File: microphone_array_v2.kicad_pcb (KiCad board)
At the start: 4 copper layers, 120 x 120 mm, 134 parts, among them J1 RPi_P1_26, J2 Tang_Nano_9K, J3 Tang_Nano_9K, U1 LP5907MFX-3.3, U2 SN74LVC244A, U3 USBLC6-4SC6, U4 USBLC6-4SC6, X1 24.576MHz

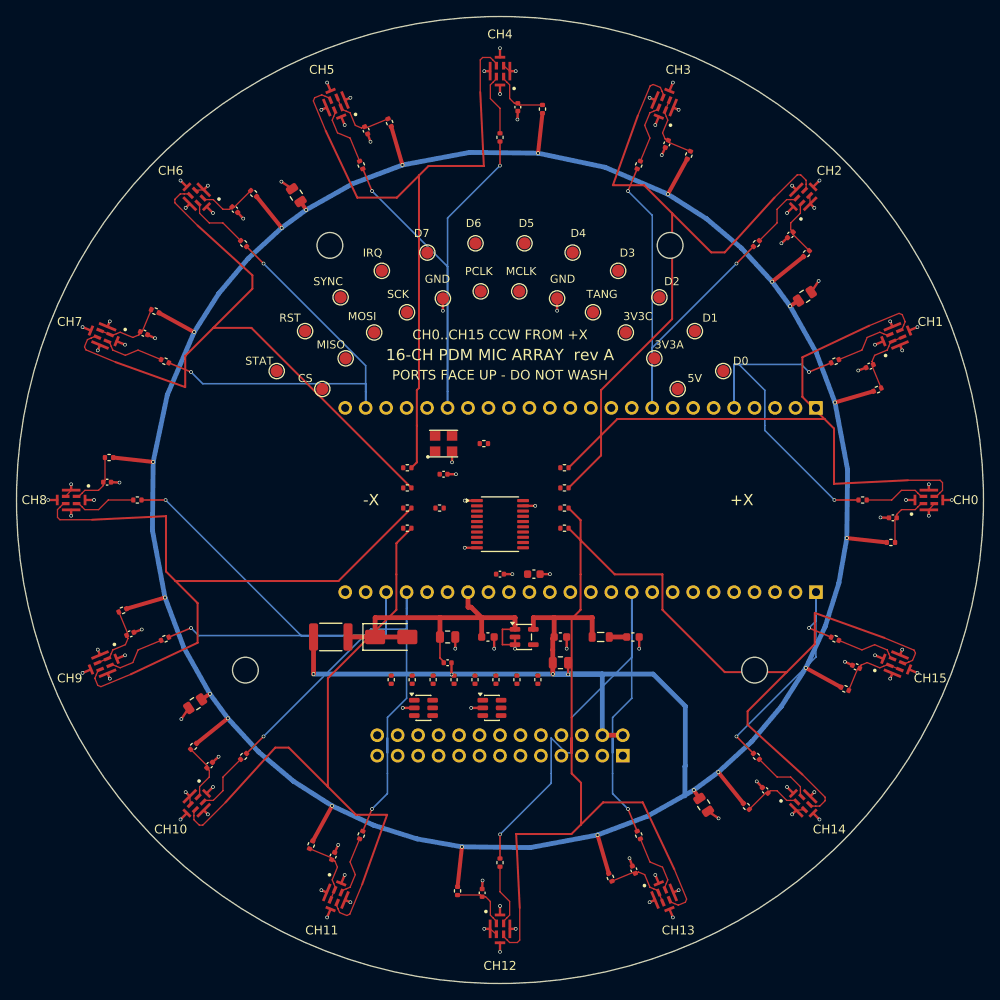
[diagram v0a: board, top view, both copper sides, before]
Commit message: Asked Claude to remove routes that hit each other, then it ran out of tokens
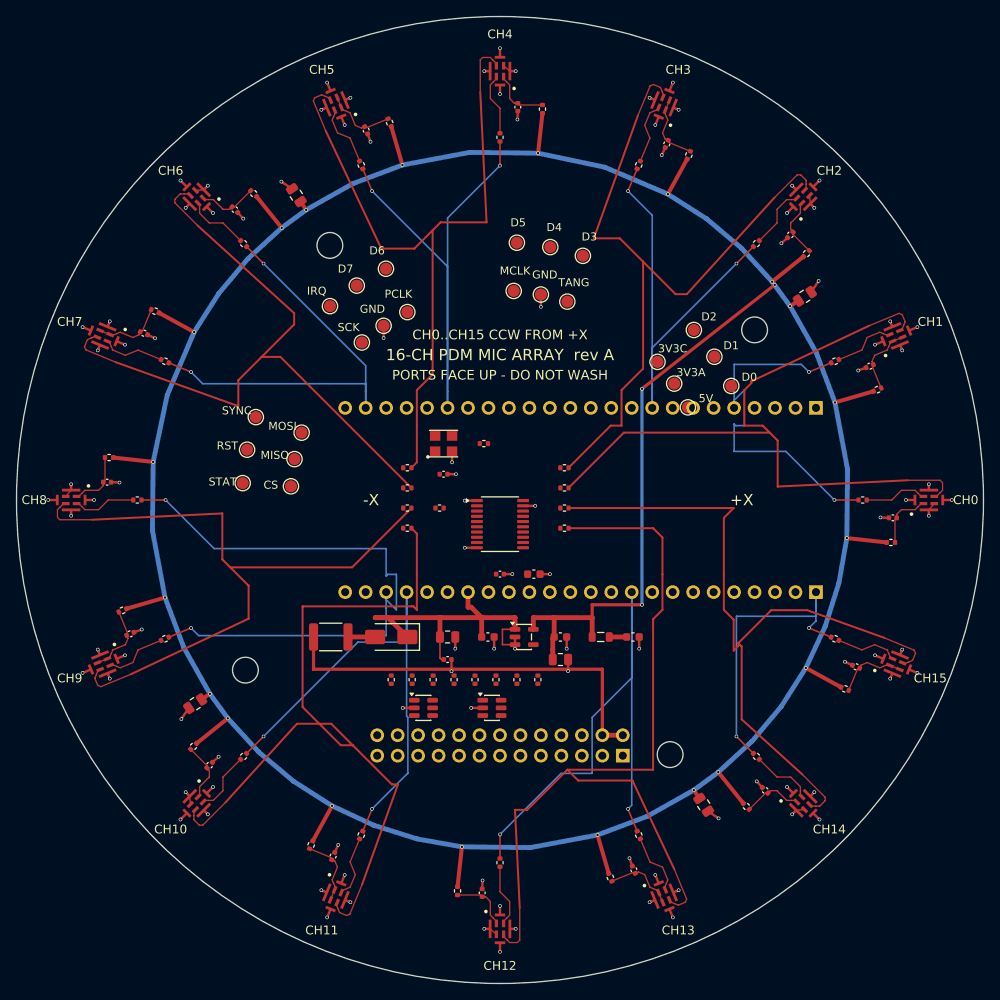
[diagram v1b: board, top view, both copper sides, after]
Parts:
- moved TP22 18.2 mm to (119.7, 139.7)
- moved TP23 16.4 mm to (118.6, 143.8)
- moved TP10 15.4 mm to (125.4, 141.6)
- moved H1 14.8 mm to (181.6, 128.9)
- moved H4 14.8 mm to (171.1, 181.6)
- moved TP24 14.5 mm to (118.1, 147.9)
- moved TP11 14.0 mm to (124.5, 144.9)
- moved TP12 12.7 mm to (124.1, 148.3)
- moved TP19 11.6 mm to (135.8, 121.3)
- moved TP20 9.67 mm to (132.2, 123.4)
- moved TP7 9.47 mm to (138.5, 126.7)
- moved TP8 8.10 mm to (135.6, 128.4)
- moved TP21 7.79 mm to (128.9, 125.9)
- moved TP9 6.74 mm to (132.9, 130.5)
- moved TP15 5.89 mm to (174.1, 128.9)
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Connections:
- U2 pad 12: PDM_CLK_Y7 -> PDM_CLK_Y6
- U2 pad 14: PDM_CLK_Y6 -> PDM_CLK_Y7
- U2 pad 16: PDM_CLK_Y1 -> PDM_CLK_Y0
- U2 pad 18: PDM_CLK_Y0 -> PDM_CLK_Y1
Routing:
- net +3V3A: track 404.1 -> 431.0 mm, vias 21 -> 23
- net PDM_CLK_B5: track 85.5 -> 100.9 mm
- net PDM_CLK_B6: track 93.7 -> 107.0 mm
- net PDM_CLK_B7: track 86.2 -> 94.0 mm
- net PDM_D6: track 79.3 -> 72.2 mm
- net PDM_CLK_B0: track 83.4 -> 90.1 mm
- net PDM_D7: track 32.8 -> 38.6 mm
- net PDM_CLK_B2: track 85.8 -> 90.8 mm
- net 5V_FUSED: track 7.36 -> 3.36 mm
- net PDM_CLK_B3: track 81.9 -> 85.5 mm
- net PDM_CLK_B4: track 82.1 -> 85.7 mm
- net PDM_D5: track 66.3 -> 63.6 mm
- net +5V: track 38.5 -> 40.9 mm
- net PDM_D4: track 75.7 -> 77.7 mm
- net PDM_CLK_B1: track 88.5 -> 90.4 mm
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
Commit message: Used auto router and removed test pads
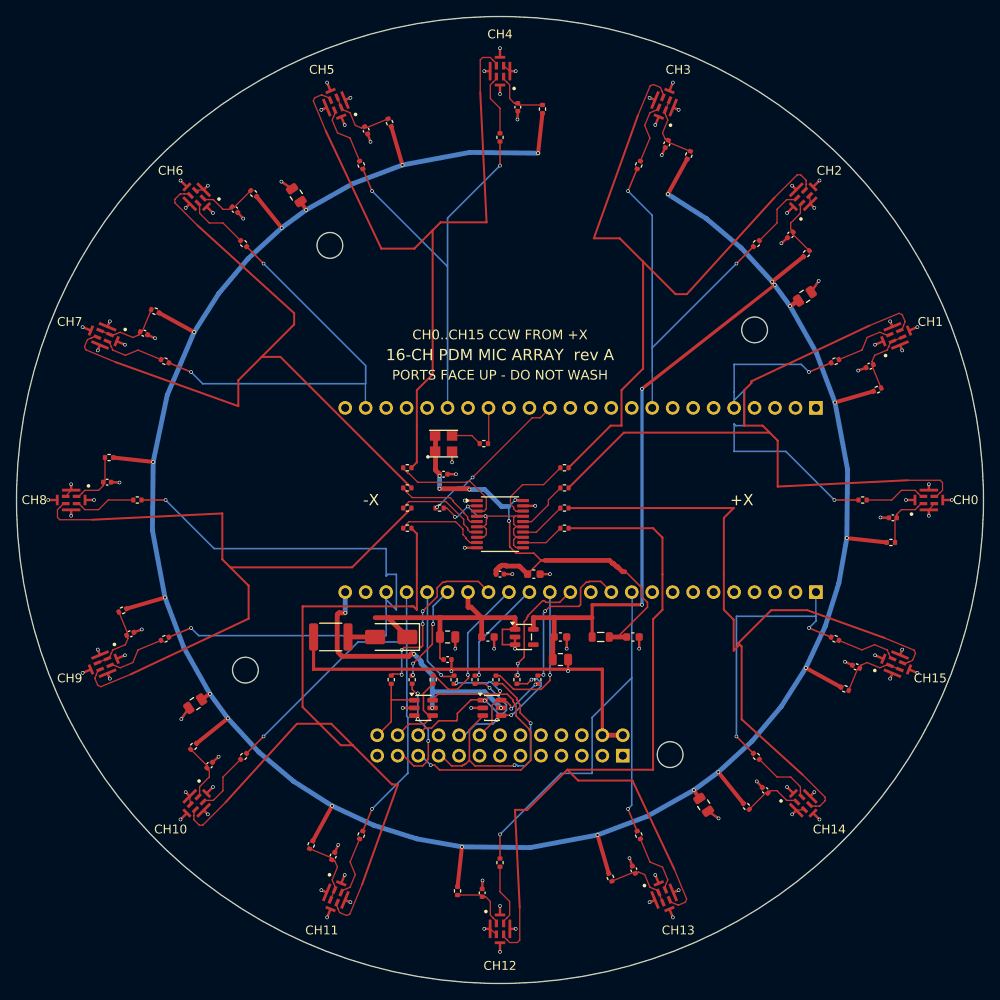
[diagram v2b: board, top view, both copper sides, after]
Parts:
- removed TP1: +5V, TestPoint:TestPoint_Pad_D1.5mm
- removed TP10: SPI_MOSI, TestPoint:TestPoint_Pad_D1.5mm
- removed TP11: SPI_MISO, TestPoint:TestPoint_Pad_D1.5mm
- removed TP12: SPI_CS_N, TestPoint:TestPoint_Pad_D1.5mm
- removed TP13: PDM_D0, TestPoint:TestPoint_Pad_D1.5mm
- removed TP14: PDM_D1, TestPoint:TestPoint_Pad_D1.5mm
- removed TP15: PDM_D2, TestPoint:TestPoint_Pad_D1.5mm
- removed TP16: PDM_D3, TestPoint:TestPoint_Pad_D1.5mm
- removed TP17: PDM_D4, TestPoint:TestPoint_Pad_D1.5mm
- removed TP18: PDM_D5, TestPoint:TestPoint_Pad_D1.5mm
- removed TP19: PDM_D6, TestPoint:TestPoint_Pad_D1.5mm
- removed TP2: +3V3A, TestPoint:TestPoint_Pad_D1.5mm
- removed TP20: PDM_D7, TestPoint:TestPoint_Pad_D1.5mm
- removed TP21: HOST_IRQ, TestPoint:TestPoint_Pad_D1.5mm
- removed TP22: HOST_SYNC, TestPoint:TestPoint_Pad_D1.5mm
- removed TP23: HOST_RESET_N, TestPoint:TestPoint_Pad_D1.5mm
- removed TP24: HOST_STATUS, TestPoint:TestPoint_Pad_D1.5mm
- removed TP3: +3V3_CLK, TestPoint:TestPoint_Pad_D1.5mm
- removed TP4: TANG_3V3, TestPoint:TestPoint_Pad_D1.5mm
- removed TP5, TP8: GND, TestPoint:TestPoint_Pad_D1.5mm
- removed TP6: AUDIO_MCLK, TestPoint:TestPoint_Pad_D1.5mm
- removed TP7: PDM_CLK_IN, TestPoint:TestPoint_Pad_D1.5mm
- removed TP9: SPI_SCLK, TestPoint:TestPoint_Pad_D1.5mm
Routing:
- net +3V3_CLK: track 2.16 -> 60.1 mm, vias 0 -> 5
- net PI_MISO: track 0.00 -> 40.5 mm, vias 0 -> 3
- net TANG_3V3: track 0.00 -> 35.1 mm, vias 0 -> 4
- net PI_MOSI: track 0.00 -> 30.6 mm, vias 0 -> 2
- net PDM_CLK_IN: track 0.00 -> 27.1 mm, vias 0 -> 3
- net HOST_RESET_N: track 0.00 -> 22.5 mm, vias 0 -> 4
- net HOST_SYNC: track 0.00 -> 20.2 mm, vias 0 -> 2
- net PI_IRQ: track 0.00 -> 19.8 mm, vias 0 -> 2
- net PDM_CLK_FPGA: track 0.00 -> 19.2 mm, vias 0 -> 2
- net SPI_MOSI: track 0.00 -> 18.9 mm, vias 0 -> 1
- net SPI_CS_N: track 0.00 -> 18.5 mm, vias 0 -> 1
- net +3V3A: track 431.0 -> 412.9 mm
- net PDM_D2: track 69.5 -> 52.0 mm
- net PI_STATUS: track 0.00 -> 16.6 mm, vias 0 -> 3
- net PI_SCLK: track 0.00 -> 15.9 mm, vias 0 -> 3
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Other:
- board text removed: "3V3A"
- board text removed: "3V3C"
- board text removed: "5V"
- board text removed: "CS"
- board text removed: "D0"
- board text removed: "D1"
- board text removed: "D2"
- board text removed: "D3"
- board text removed: "D4"
- board text removed: "D5"
- board text removed: "D6"
- board text removed: "D7"
- board text removed: "GND"
- board text removed: "IRQ"
- board text removed: "MCLK"
- board text removed: "MISO"
- board text removed: "MOSI"
- board text removed: "PCLK"
- board text removed: "RST"
- board text removed: "SCK"
- board text removed: "STAT"
- board text removed: "SYNC"
- board text removed: "TANG"

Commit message: Claude fixup
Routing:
- net GND: track 113.0 -> 111.3 mm
- net +5V: track 39.3 -> 37.7 mm
- net +3V3A: track 412.9 -> 412.6 mm, vias 23 -> 22

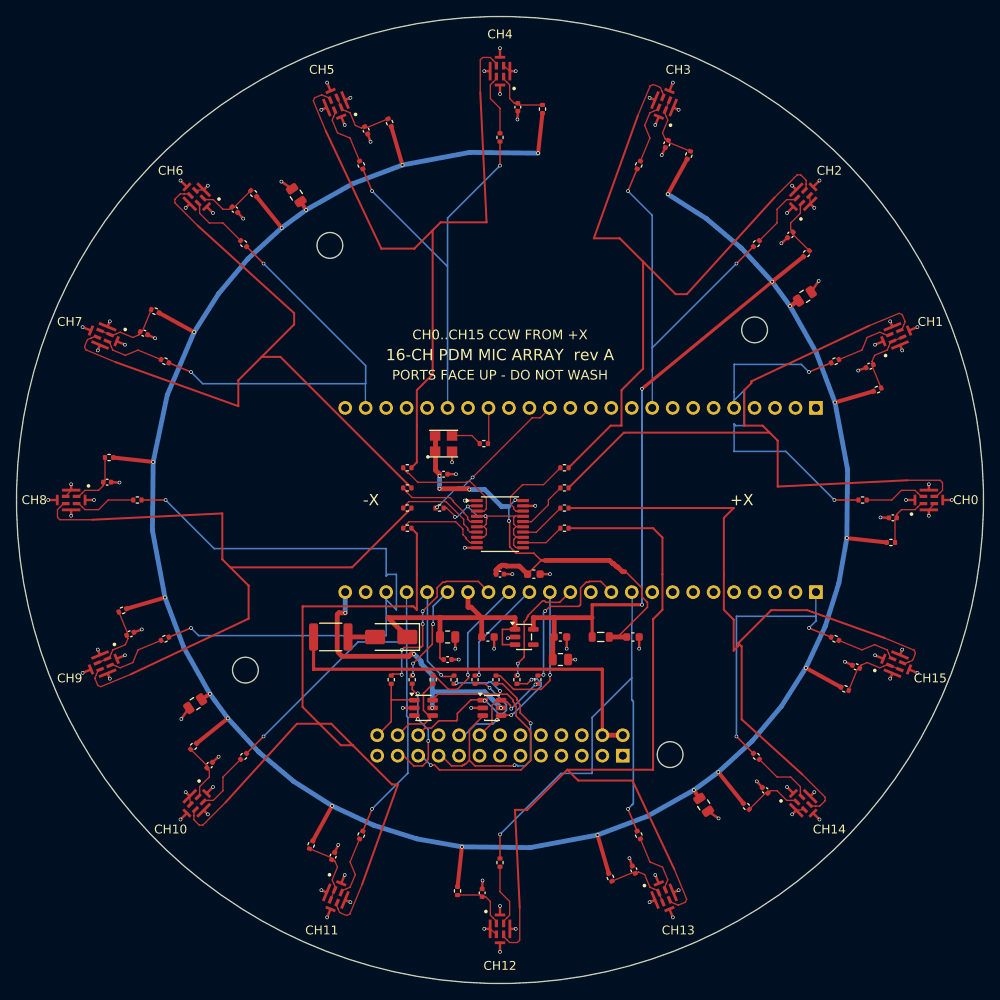
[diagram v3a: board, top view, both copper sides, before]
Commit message: Placed test points, generated release
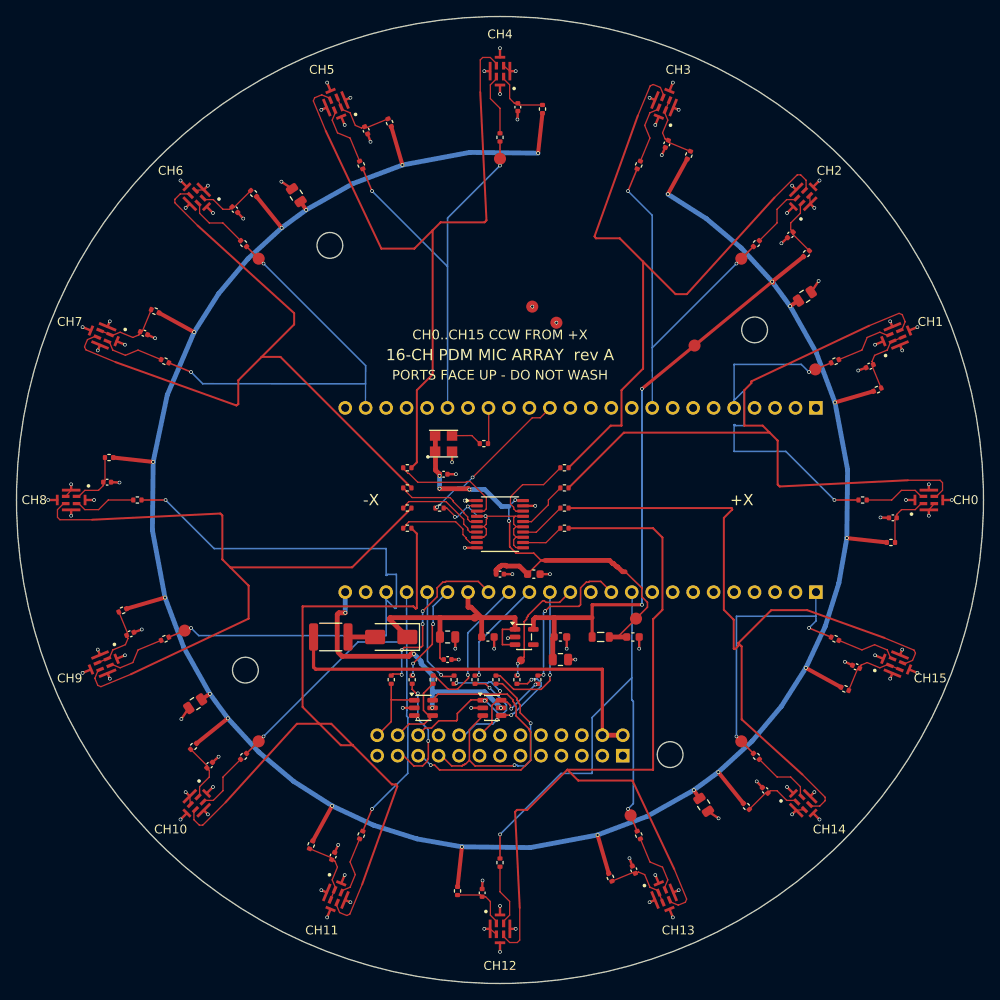
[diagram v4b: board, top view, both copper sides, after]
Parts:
- added TP1: +5V, MicArrayV2:TestPoint_Pad_D1.0mm_NoSilk, F.Cu at (146.9, 164.6)
- added TP10: PDM_D4, MicArrayV2:TestPoint_Pad_D1.5mm_NoSilk, F.Cu at (110.9, 166.2)
- added TP11: PDM_D5, MicArrayV2:TestPoint_Pad_D1.5mm_NoSilk, F.Cu at (120.1, 179.9)
- added TP12: PDM_D6, MicArrayV2:TestPoint_Pad_D1.5mm_NoSilk, F.Cu at (166.2, 189.1)
- added TP13: PDM_D7, MicArrayV2:TestPoint_Pad_D1.5mm_NoSilk, F.Cu at (179.9, 179.9)
- added TP14: HOST_STATUS, MicArrayV2:TestPoint_Pad_D1.0mm_NoSilk, F.Cu at (152.6, 169.9)
- added TP2: +3V3A, MicArrayV2:TestPoint_Pad_D1.5mm_NoSilk, F.Cu at (174.1, 130.8)
- added TP3: +3V3_CLK, MicArrayV2:TestPoint_Pad_D1.5mm_NoSilk, F.Cu at (166.9, 164.7)
- added TP4: GND, MicArrayV2:TestPoint_Pad_D1.5mm_NoSilk, F.Cu at (154.0, 126.0)
- added TP5: GND, MicArrayV2:TestPoint_Pad_D1.5mm_NoSilk, F.Cu at (157.0, 128.0)
- added TP6: PDM_D0, MicArrayV2:TestPoint_Pad_D1.5mm_NoSilk, F.Cu at (189.1, 133.8)
- added TP7: PDM_D1, MicArrayV2:TestPoint_Pad_D1.5mm_NoSilk, F.Cu at (179.9, 120.1)
- added TP8: PDM_D2, MicArrayV2:TestPoint_Pad_D1.5mm_NoSilk, F.Cu at (150.0, 107.6)
- added TP9: PDM_D3, MicArrayV2:TestPoint_Pad_D1.5mm_NoSilk, F.Cu at (120.1, 120.1)
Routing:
- net PDM_CLK_IN: track 27.1 -> 25.6 mm
- net +3V3A: track 412.6 -> 411.7 mm
- net PDM_CLK_B7: track 94.0 -> 93.4 mm
- net +3V3_CLK: track 60.1 -> 59.6 mm
- net GND: vias 100 -> 102
